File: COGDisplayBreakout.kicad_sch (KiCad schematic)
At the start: 12 parts, among them J1 FPC_12pin, J2 SPI_Header, J4 Conn_01x01, J5 Conn_01x01

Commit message: 3rd Rev send to OshPark
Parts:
- added C4: 1uF, Capacitor_SMD:C_0805_2012Metric, symbol Device:C
- C1: value 1uF -> 10uF
- R1: value 15R -> 20R
- renumbered C3 to C2, C2 to C3
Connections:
- net +3V3: now also C1.1
- net GND: now also C1.2, C4.2; no longer C3.2
- net V0: no longer C1.1
- net VG: now also C4.1
- net XV0: now also C3.2; no longer C1.2
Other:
- moved on the sheet: C1, C3

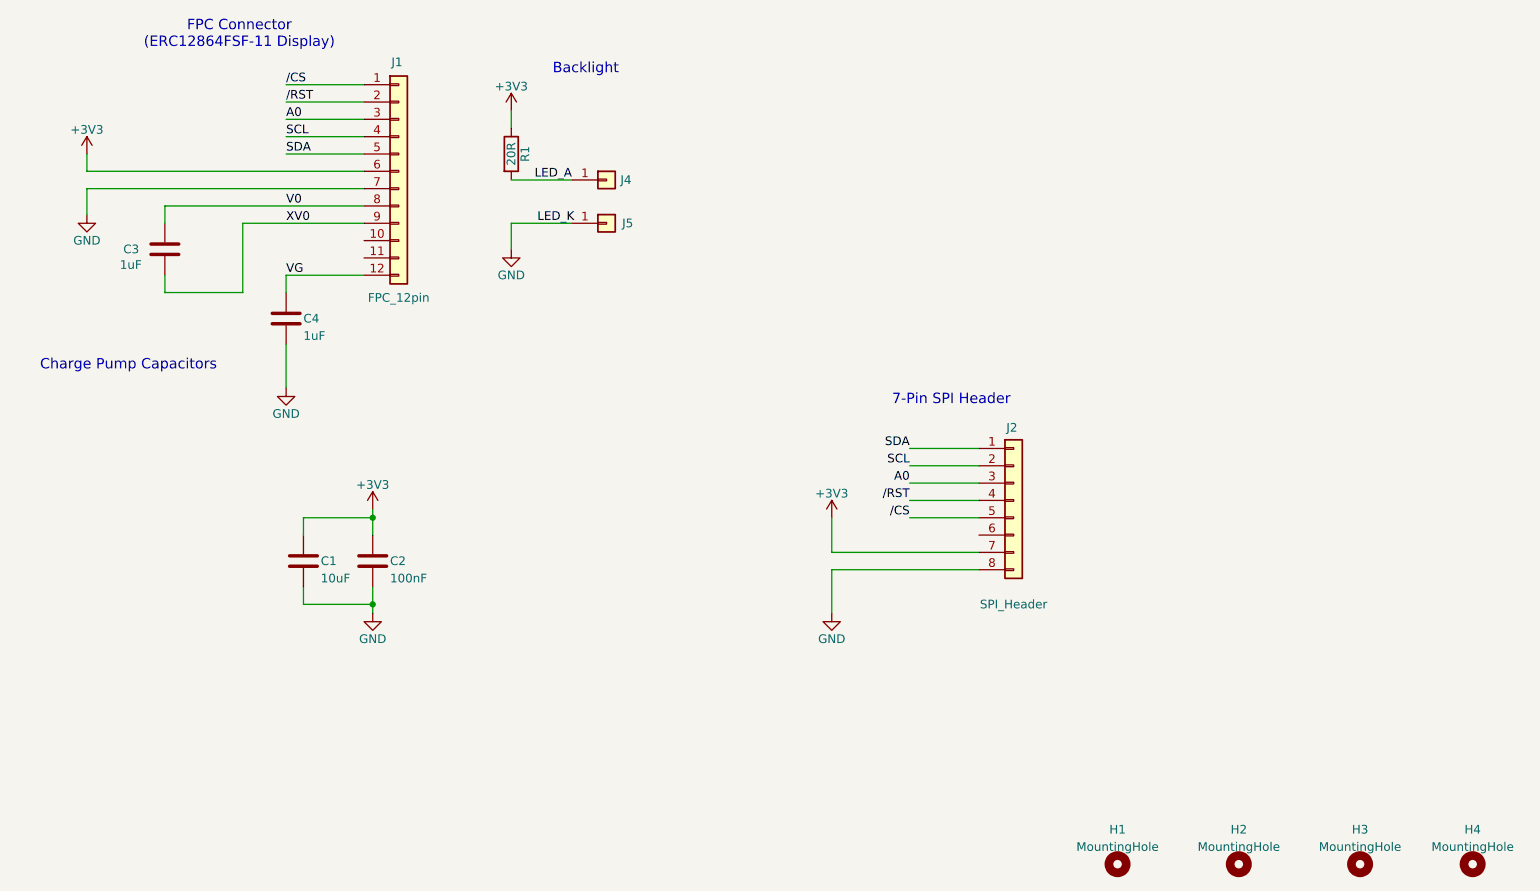
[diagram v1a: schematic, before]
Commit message: Fixes v0.2 problems, new symbol and 3D model
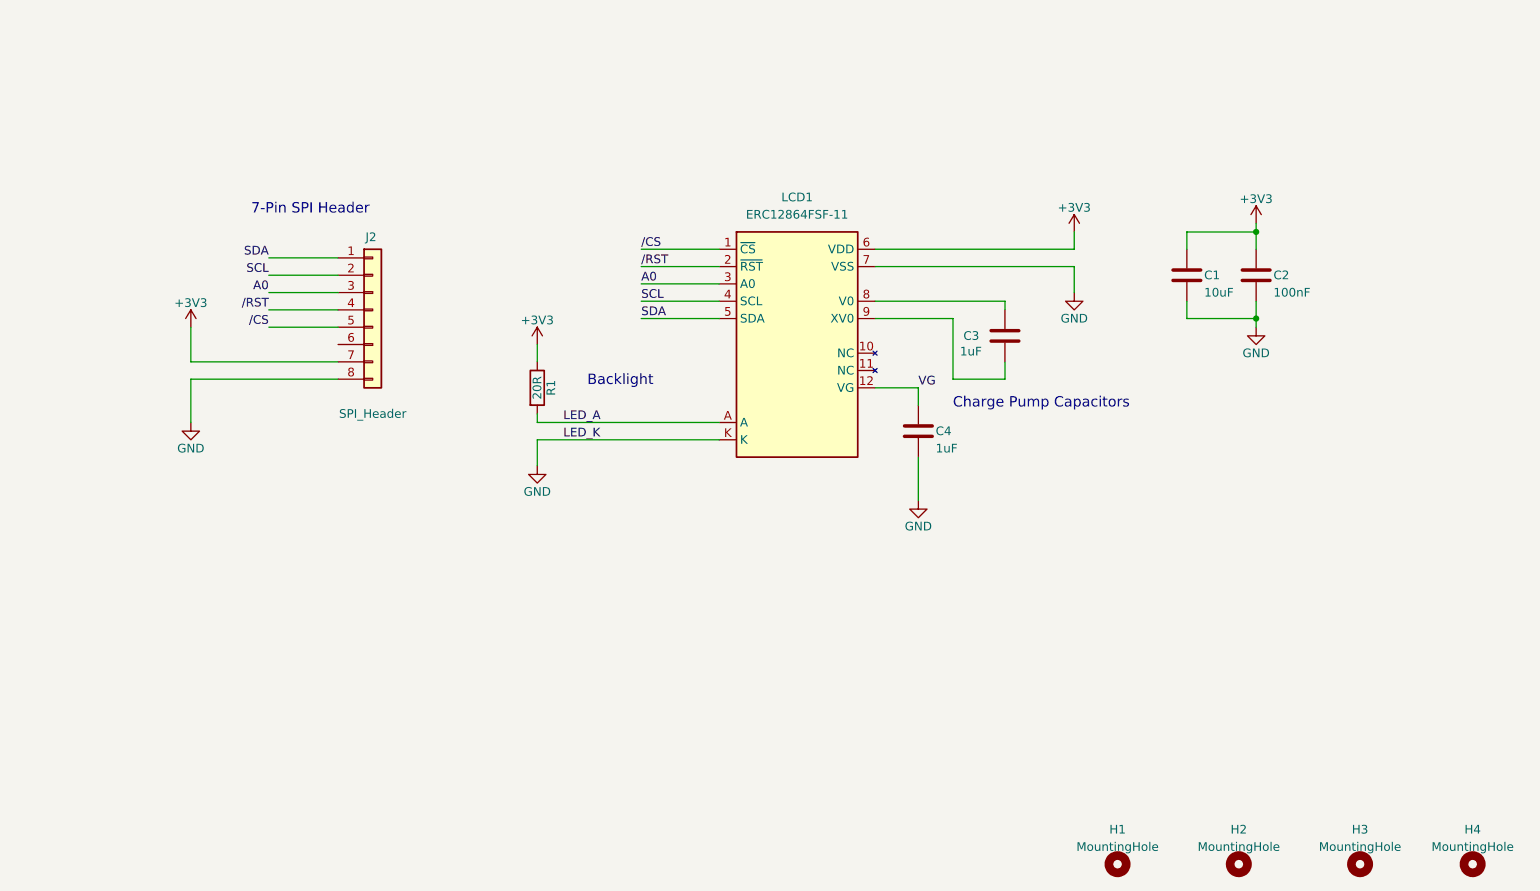
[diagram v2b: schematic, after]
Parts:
- removed J1: FPC_12pin, Connector_FFC-FPC:Hirose_FH12-12S-0.5SH_1x12-1MP_P0.50mm_Horizontal, symbol Connector_Generic:Conn_01x12
- removed J4, J5: Conn_01x01, Connector_PinHeader_2.54mm:PinHeader_1x01_P2.54mm_Vertical, symbol Connector_Generic:Conn_01x01
- added LCD1: ERC12864FSF-11, COGDisplayBreakout:ERC12864FSF-11_COG_LCD, symbol COGDisplayBreakout:ERC12864FSF-11
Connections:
- net +3V3: now also LCD1.6 (VDD)
- net /CS: now also LCD1.1 (~{CS})
- net /RST: now also LCD1.2 (~{RST})
- net A0: now also LCD1.3 (A0)
- net GND: now also LCD1.7 (VSS), LCD1.K
- net LED_A: now also LCD1.A
- net SCL: now also LCD1.4 (SCL)
- net SDA: now also LCD1.5 (SDA)
- net VG: now also LCD1.12 (VG)
- net V0: no longer names the net of C3.1
- net V0: now also LCD1.8 (V0)
- net XV0: no longer names the net of C3.2
- net XV0: now also LCD1.9 (XV0)
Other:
- note removed: "FPC Connector (ERC12864FSF-11 Display)"
- moved on the sheet: C1, C2, J2

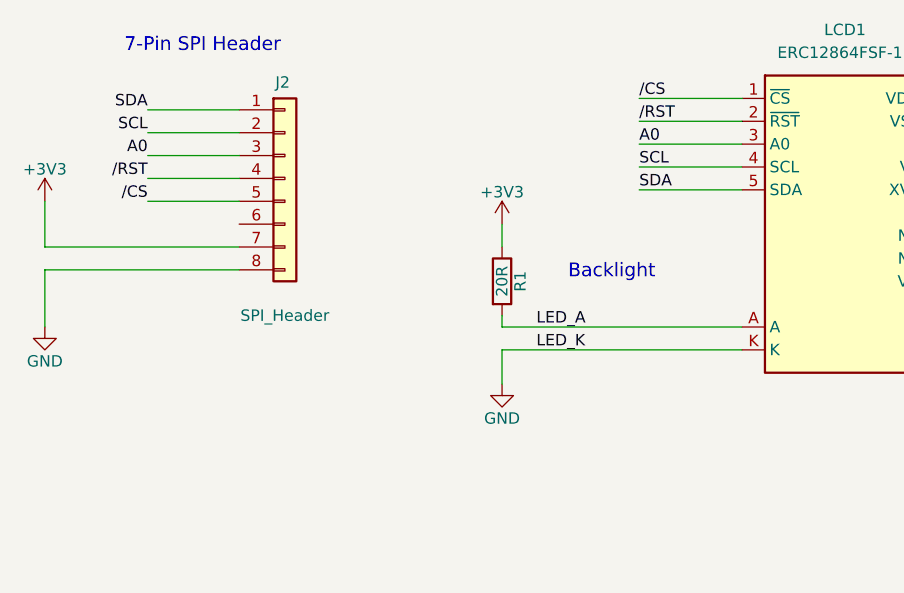
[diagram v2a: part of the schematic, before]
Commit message: Rewired LED: fix A/K swap and adds control from pin 6
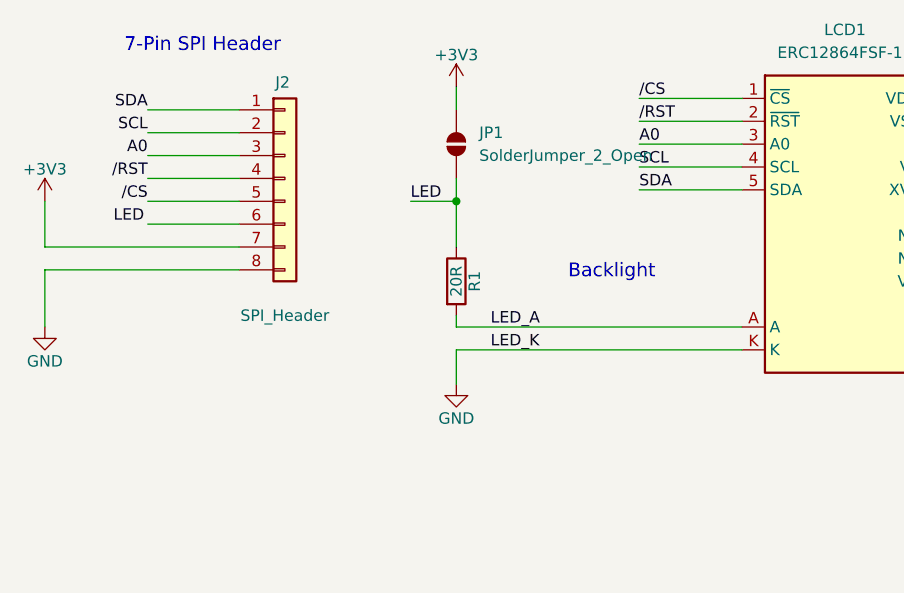
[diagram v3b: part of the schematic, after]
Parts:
- added JP1: SolderJumper_2_Open, Jumper:SolderJumper-2_P1.3mm_Open_RoundedPad1.0x1.5mm, symbol Jumper:SolderJumper_2_Open
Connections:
- net +3V3: now also JP1.2 (B); no longer R1.1
- new net LED: JP1.1 (A), R1.1
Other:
- moved on the sheet: R1
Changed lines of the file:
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@@
+	)
+	(junction
+		(at 116.84 81.28)
+		(diameter 0)
+		(color 0 0 0 0)
 	)
 	(junction
@@
 	(wire
 		(pts
-			(xy 148.59 95.25) (xy 121.92 95.25)
+			(xy 148.59 95.25) (xy 116.84 95.25)
+		)
+		(stroke
+			(width 0)
+			(type default)
+		)
+	)
+	(wire
+		(pts
+			(xy 116.84 81.28) (xy 116.84 86.36)
 		)
 		(stroke
@@
 	(wire
 		(pts
-			(xy 121.92 95.25) (xy 121.92 93.98)
+			(xy 116.84 95.25) (xy 116.84 93.98)
 		)
 		(stroke
@@
 	(wire
 		(pts
-			(xy 121.92 97.79) (xy 121.92 101.6)
+			(xy 116.84 97.79) (xy 116.84 101.6)
 		)
 		(stroke
@@
 	(wire
 		(pts
+			(xy 111.76 81.28) (xy 116.84 81.28)
+		)
+		(stroke
+			(width 0)
+			(type default)
+		)
+	)
+	(wire
+		(pts
 			(xy 92.71 71.12) (xy 82.55 71.12)
 		)
@@
 	(wire
 		(pts
+			(xy 116.84 71.12) (xy 116.84 68.58)
+		)
+		(stroke
+			(width 0)
+			(type default)
+		)
+	)
+	(wire
+		(pts
 			(xy 171.45 77.47) (xy 190.5 77.47)
 		)
@@
 	(wire
 		(pts
-			(xy 121.92 97.79) (xy 148.59 97.79)
+			(xy 116.84 97.79) (xy 148.59 97.79)
+		)
+		(stroke
+			(width 0)
+			(type default)
+		)
+	)
+	(wire
+		(pts
+			(xy 82.55 83.82) (xy 92.71 83.82)
 		)
 		(stroke
@@
 	(wire
 		(pts
-			(xy 121.92 83.82) (xy 121.92 86.36)
+			(xy 116.84 78.74) (xy 116.84 81.28)
 		)
 		(stroke
@@
 		)
 	)
+	(label "LED"
+		(at 111.76 81.28 0)
+		(effects
+			(font
+				(size 1.27 1.27)
+			)
+			(justify left bottom)
+		)
+	)
 	(label "LED_K"
-		(at 125.73 97.79 0)
+		(at 120.65 97.79 0)
 		(effects
 			(font
@@
 	)
 	(label "LED_A"
-		(at 125.73 95.25 0)
+		(at 120.65 95.25 0)
 		(effects
 			(font
@@
 	(label "/RST"
 		(at 137.16 72.39 0)
+		(effects
+			(font
+				(size 1.27 1.27)
+			)
+			(justify left bottom)
+		)
+	)
+	(label "LED"
+		(at 78.74 83.82 0)
 		(effects
 			(font
@@
 	)
 	(symbol
+		(lib_id "Jumper:SolderJumper_2_Open")
+		(at 116.84 74.93 90)
+		(unit 1)
+		(exclude_from_sim no)
+		(in_bom no)
+		(on_board yes)
+		(dnp no)
+		(fields_autoplaced yes)
+		(property "Reference" "JP1"
+			(at 119.38 73.6599 90)
+			(effects
+				(font
+					(size 1.27 1.27)
+				)
+				(justify right)
+			)
+		)
+		(property "Value" "SolderJumper_2_Open"
+			(at 119.38 76.1999 90)
+			(effects
+				(font
+					(size 1.27 1.27)
+				)
+				(justify right)
+			)
+		)
+		(property "Footprint" "Jumper:SolderJumper-2_P1.3mm_Open_RoundedPad1.0x1.5mm"
+			(at 116.84 74.93 0)
+			(effects
+				(font
+					(size 1.27 1.27)
+				)
+				(hide yes)
+			)
+		)
+		(property "Datasheet" "~"
+			(at 116.84 74.93 0)
+			(effects
+				(font
+					(size 1.27 1.27)
+				)
+				(hide yes)
+			)
+		)
+		(property "Description" "Solder Jumper, 2-pole, open"
+			(at 116.84 74.93 0)
+			(effects
+				(font
+					(size 1.27 1.27)
+				)
+				(hide yes)
+			)
+		)
+		(pin "2"
+		)
+		(pin "1"
+		)
+		(instances
+			(project ""
+				(path "/5d6668f5-9efd-4633-a357-e3746984ef57"
+					(reference "JP1")
+					(unit 1)
+				)
+			)
+		)
+	)
+	(symbol
 		(lib_id "Device:R")
-		(at 121.92 90.17 0)
+		(at 116.84 90.17 0)
 		(unit 1)
 		(exclude_from_sim no)
@@
 		(dnp no)
 		(property "Reference" "R1"
-			(at 123.952 90.17 90)
+			(at 118.872 90.17 90)
 			(effects
 				(font
@@
 		)
 		(property "Value" "20R"
-			(at 121.92 90.17 90)
+			(at 116.84 90.17 90)
 			(effects
 				(font
@@
 		)
 		(property "Footprint" "Resistor_SMD:R_0805_2012Metric"
-			(at 120.142 90.17 90)
+			(at 115.062 90.17 90)
 			(effects
 				(font
@@
 		)
 		(property "Datasheet" "~"
-			(at 121.92 90.17 0)
+			(at 116.84 90.17 0)
 			(effects
 				(font
@@
 		)
 		(property "Description" "Backlight LED current limiting resistor"
-			(at 121.92 90.17 0)
+			(at 116.84 90.17 0)
 			(effects
 				(font
@@
 	)
 	(symbol
+		(lib_id "power:GND")
+		(at 116.84 101.6 0)
+		(unit 1)
+		(exclude_from_sim no)
+		(in_bom yes)
+		(on_board yes)
+		(dnp no)
+		(property "Reference" "#PWR07"
+			(at 116.84 107.95 0)
+			(effects
+				(font
+					(size 1.27 1.27)
+				)
+				(hide yes)
+			)
+		)
+		(property "Value" "GND"
+			(at 116.84 105.41 0)
+			(effects
+				(font
+					(size 1.27 1.27)
+				)
+			)
+		)
+		(property "Footprint" ""
+			(at 116.84 101.6 0)
+			(effects
+				(font
+					(size 1.27 1.27)
+				)
+				(hide yes)
+			)
+		)
+		(property "Datasheet" ""
+			(at 116.84 101.6 0)
+			(effects
+				(font
+					(size 1.27 1.27)
+				)
+				(hide yes)
+			)
+		)
+		(property "Description" ""
+			(at 116.84 101.6 0)
+			(effects
+				(font
+					(size 1.27 1.27)
+				)
+				(hide yes)
+			)
+		)
+		(pin "1"
+		)
+		(instances
+			(project "COGDisplayBreakout"
+				(path "/5d6668f5-9efd-4633-a357-e3746984ef57"
+					(reference "#PWR07")
+					(unit 1)
+				)
+			)
+		)
+	)
+	(symbol
 		(lib_id "power:+3V3")
-		(at 121.92 83.82 0)
+		(at 116.84 68.58 0)
 		(unit 1)
 		(exclude_from_sim no)
@@
 		(dnp no)
 		(property "Reference" "#PWR01"
-			(at 121.92 87.63 0)
+			(at 116.84 72.39 0)
 			(effects
 				(font
@@
 		)
 		(property "Value" "+3V3"
-			(at 121.92 80.264 0)
+			(at 116.84 65.024 0)
 			(effects
 				(font
@@
 		)
 		(property "Footprint" ""
-			(at 121.92 83.82 0)
+			(at 116.84 68.58 0)
 			(effects
 				(font
@@
 		)
 		(property "Datasheet" ""
-			(at 121.92 83.82 0)
+			(at 116.84 68.58 0)
 			(effects
 				(font
@@
 		)
 		(property "Description" ""
-			(at 121.92 83.82 0)
+			(at 116.84 68.58 0)
 			(effects
 				(font
@@
 					(unit 1)
 				)
-			)
-		)
-	)
-	(symbol
-		(lib_id "power:GND")
-		(at 121.92 101.6 0)
-		(unit 1)
-		(exclude_from_sim no)
-		(in_bom yes)
-		(on_board yes)
-		(dnp no)
-		(property "Reference" "#PWR07"
-			(at 121.92 107.95 0)
-			(effects
-				(font
-					(size 1.27 1.27)
-				)
-				(hide yes)
-			)
-		)
-		(property "Value" "GND"
-			(at 121.92 105.41 0)
-			(effects
-				(font
-					(size 1.27 1.27)
-				)
-			)
-		)
-		(property "Footprint" ""
-			(at 121.92 101.6 0)
-			(effects
-				(font
-					(size 1.27 1.27)
-				)
-				(hide yes)
-			)
-		)
-		(property "Datasheet" ""
-			(at 121.92 101.6 0)
-			(effects
-				(font
-					(size 1.27 1.27)
-				)
-				(hide yes)
-			)
-		)
-		(property "Description" ""
-			(at 121.92 101.6 0)
-			(effects
-				(font
-					(size 1.27 1.27)
-				)
-				(hide yes)
-			)
-		)
-		(pin "1"
-		)
-		(instances
-			(project "COGDisplayBreakout"
-				(path "/5d6668f5-9efd-4633-a357-e3746984ef57"
-					(reference "#PWR07")
-					(unit 1)
-				)

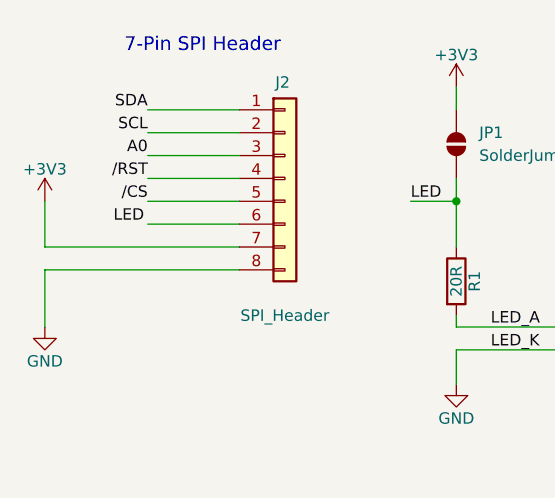
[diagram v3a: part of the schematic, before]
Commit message: Ensure Handsolder 0805 footprints
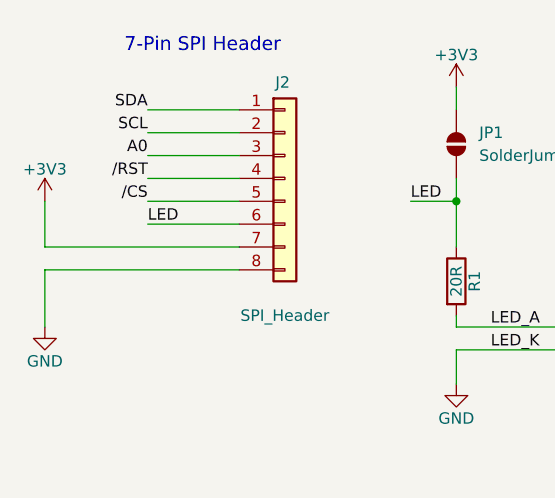
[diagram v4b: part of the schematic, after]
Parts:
- C1, C2, C3, C4: footprint Capacitor_SMD:C_0805_2012Metric -> Capacitor_SMD:C_0805_2012Metric_Pad1.18x1.45mm_HandSolder
- R1: footprint Resistor_SMD:R_0805_2012Metric -> Resistor_SMD:R_0805_2012Metric_Pad1.20x1.40mm_HandSolder
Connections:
- net LED: now also J2.6 (Pin_6)
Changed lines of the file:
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@@
+	(wire
+		(pts
+			(xy 82.55 83.82) (xy 92.71 83.82)
+		)
+		(stroke
+			(width 0)
+			(type default)
+		)
+	)
 	(wire
 		(pts
@@
 		(pts
 			(xy 116.84 97.79) (xy 148.59 97.79)
-		)
-		(stroke
-			(width 0)
-			(type default)
-		)
-	)
-	(wire
-		(pts
-			(xy 82.55 83.82) (xy 92.71 83.82)
 		)
 		(stroke
@@
 		)
 	)
+	(label "LED"
+		(at 82.55 83.82 0)
+		(effects
+			(font
+				(size 1.27 1.27)
+			)
+			(justify left bottom)
+		)
+	)
 	(label "SCL"
 		(at 82.55 73.66 180)
@@
 		)
 	)
-	(label "LED"
-		(at 78.74 83.82 0)
-		(effects
-			(font
-				(size 1.27 1.27)
-			)
-			(justify left bottom)
-		)
-	)
 	(label "SDA"
 		(at 137.16 80.01 0)
@@
 			)
 		)
-		(property "Footprint" "Resistor_SMD:R_0805_2012Metric"
+		(property "Footprint" "Resistor_SMD:R_0805_2012Metric_Pad1.20x1.40mm_HandSolder"
 			(at 115.062 90.17 90)
 			(effects
@@
 			)
 		)
-		(property "Footprint" "Capacitor_SMD:C_0805_2012Metric"
+		(property "Footprint" "Capacitor_SMD:C_0805_2012Metric_Pad1.18x1.45mm_HandSolder"
 			(at 191.4652 86.36 0)
 			(effects
@@
 			)
 		)
-		(property "Footprint" "Capacitor_SMD:C_0805_2012Metric"
+		(property "Footprint" "Capacitor_SMD:C_0805_2012Metric_Pad1.18x1.45mm_HandSolder"
 			(at 218.1352 77.47 0)
 			(effects
@@
 			)
 		)
-		(property "Footprint" "Capacitor_SMD:C_0805_2012Metric"
+		(property "Footprint" "Capacitor_SMD:C_0805_2012Metric_Pad1.18x1.45mm_HandSolder"
 			(at 228.2952 77.47 0)
 			(effects
@@
 			)
 		)
-		(property "Footprint" "Capacitor_SMD:C_0805_2012Metric"
+		(property "Footprint" "Capacitor_SMD:C_0805_2012Metric_Pad1.18x1.45mm_HandSolder"
 			(at 178.7652 100.33 0)
 			(effects

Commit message: readme edits
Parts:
- renumbered J2 to J1
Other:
- note added: "8-Pin SPI Header"
- note removed: "7-Pin SPI Header"
- moved on the sheet: C1, C2, C3, C4, J1, JP1, LCD1, R1
